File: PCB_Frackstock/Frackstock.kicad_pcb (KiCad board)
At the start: 4 copper layers, 23 x 125.5 mm, 59 parts, among them J1 Conn_02x03_Pin, J2 105450-0101, J3 Conn_02x03_Pin, J4 Conn_02x03_Pin, J5 VBUS, U1 Pico, U11 CC1101RGPR, U14 1043, U2 BMI160, U3 MCP73871-2CC, Y2 26MHz

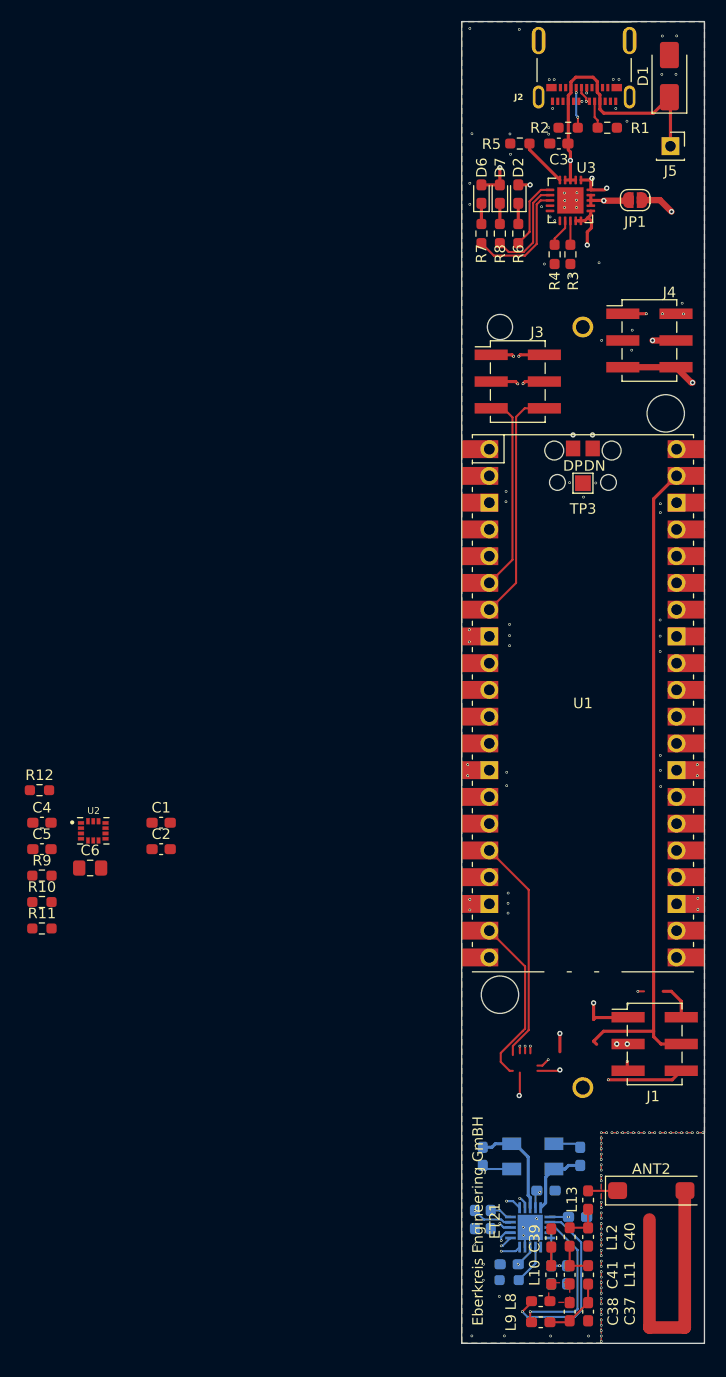
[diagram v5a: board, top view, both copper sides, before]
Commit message: Fracstock PCB final commit
DRC check, PCB review done, ready to order
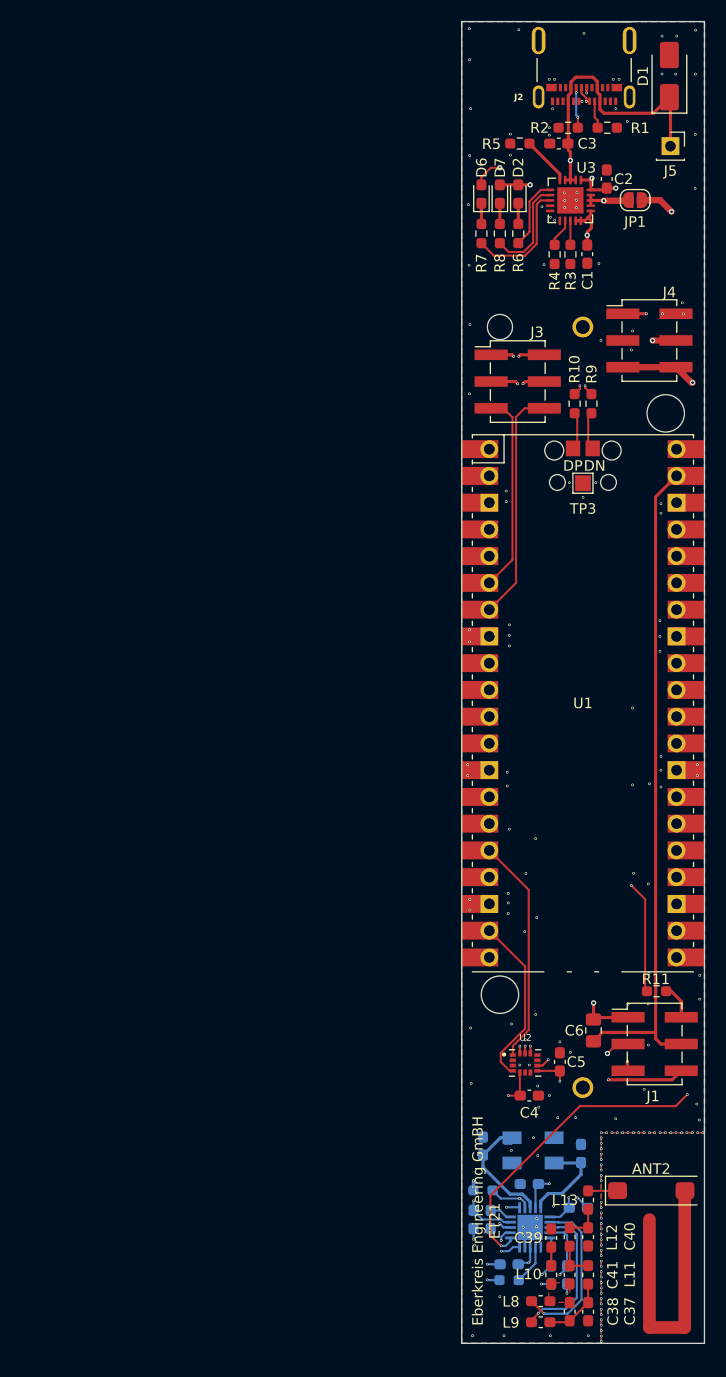
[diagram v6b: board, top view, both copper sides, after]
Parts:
- added REF**: KiCad-Logo2_6mm_SilkScreen, Symbol:KiCad-Logo2_6mm_SilkScreen, B.Cu at (130.3, 43.8)
- R12: moved to B.Cu
- moved C2 76.4 mm to (132.2, 41.6), turned to 90 degrees
- moved R10 69.3 mm to (129.1, 62.9), turned to 90 degrees
- moved R9 68.8 mm to (130.7, 62.9), turned to 90 degrees
- moved C1 67.5 mm to (130.3, 48.7), turned to -90 degrees
- moved R11 58.7 mm to (136.9, 118.7)
- moved R12 56.7 mm to (120.4, 137.6)
- moved C5 53.2 mm to (127.7, 125.4), turned to 90 degrees
- moved C4 53.0 mm to (124.8, 128.6)
- moved C6 50.2 mm to (130.9, 122.4), turned to -90 degrees
- moved U2 46.6 mm to (124.4, 125.5)
- moved C26 1.70 mm to (124.8, 137.0), turned to 180 degrees
- moved C22 0.97 mm to (120.4, 133.4), turned to 90 degrees
- moved C25 0.87 mm to (129.5, 139.2)
- moved Y2 0.57 mm to (125.2, 133.8)
- moved C30 0.28 mm to (129.7, 134.1)
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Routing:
- net +3.3V: track 45.2 -> 57.9 mm, vias 128 -> 11
- net COM_CLK: track 43.4 -> 50.9 mm, vias 1 -> 2
- net DP: track 36.5 -> 32.5 mm
- net DN: track 37.7 -> 33.8 mm
- net Net-(R9-Pad1): track 0.02 -> 3.66 mm
- net Net-(R10-Pad1): track 0.01 -> 3.61 mm
- net COM_CS: track 32.6 -> 35.7 mm
- net XOSC_Q2: track 6.84 -> 9.21 mm
- net XOSC_Q1: track 9.57 -> 11.7 mm
- net RF_P: track 17.5 -> 15.6 mm
- net VBUS: track 47.7 -> 49.4 mm
- net GND: track 39.0 -> 40.7 mm, vias 24 -> 189
- net BAT_P: track 12.9 -> 13.8 mm
- net BAT_O: track 122.0 -> 121.5 mm
- net RF_N: track 14.8 -> 14.3 mm
- added copper zone on B.Cu, net GND
- added copper zone on F.Cu, net GND
- added copper zone on In1.Cu, net GND
- removed copper zone on B.Cu, net +3.3V
- removed copper zone on F.Cu, net +3.3V
- removed copper zone on In1.Cu, net +3.3V
